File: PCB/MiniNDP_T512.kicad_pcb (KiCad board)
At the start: 2 copper layers, 60 x 34 mm, 25 parts, among them J1 Conn_02x20_Odd_Even, U1 HC238, U2 HC4040, U3 HC573, U4 AS6C4008, U5 1G79, U6 2G00

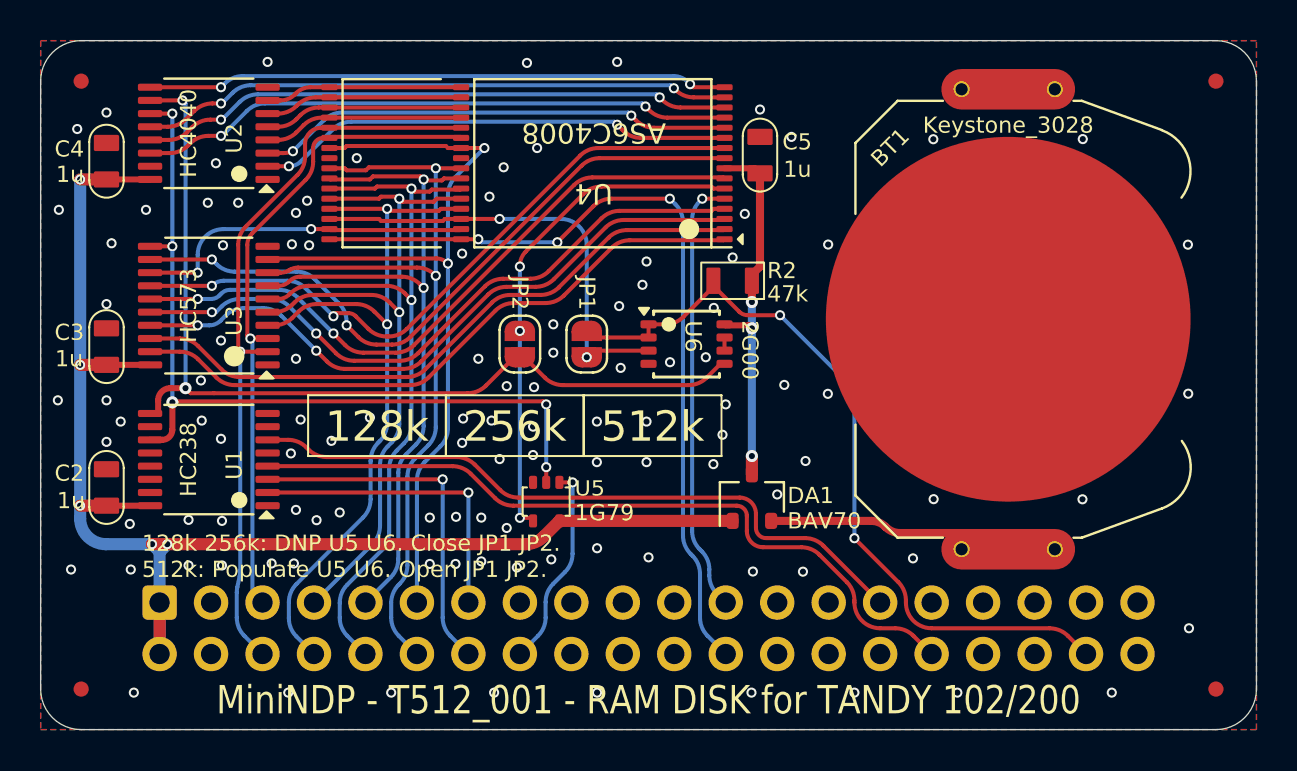
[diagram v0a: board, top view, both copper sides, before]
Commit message: T512 connect all gnd islands
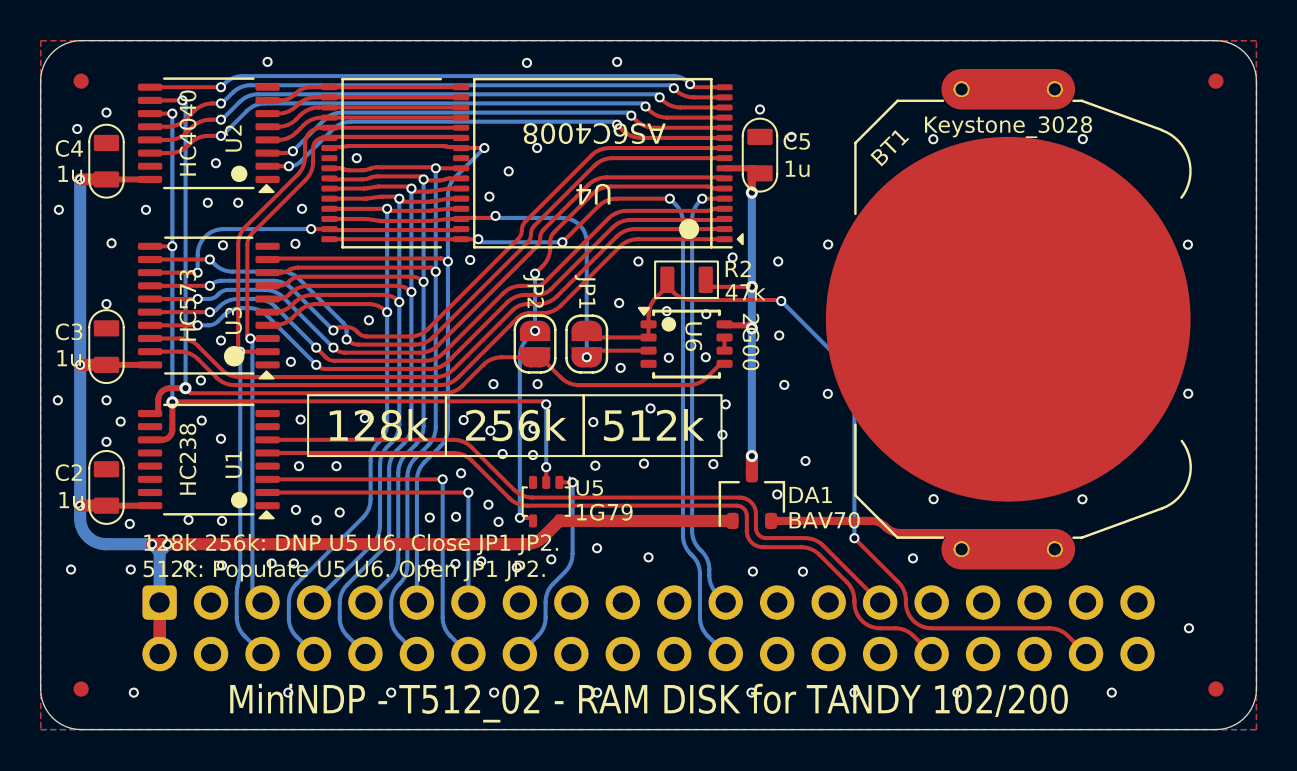
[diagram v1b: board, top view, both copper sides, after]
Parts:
- moved R2 2.28 mm to (153.8, 97.8)
- moved JP2 0.75 mm to (146.3, 101.0)
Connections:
- U1 pad 4: /(A) -> GND
- U1 pad 5: GND -> /(A)
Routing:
- net VMEM: track 18.3 -> 21.0 mm, vias 3 -> 4
- net /RAMRST: track 38.8 -> 39.9 mm
- net GND: vias 111 -> 108

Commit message: T512 power traces
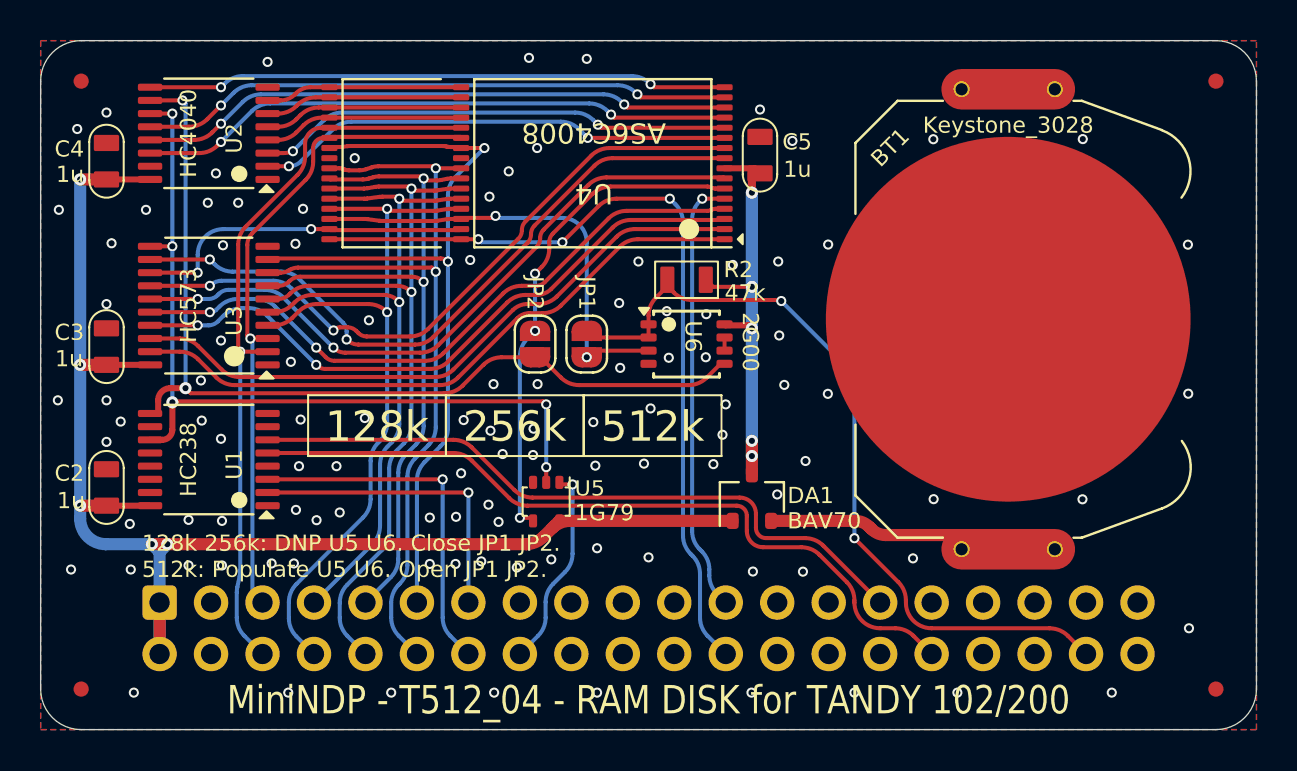
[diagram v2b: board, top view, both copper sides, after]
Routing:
- net +BATT: track 14.5 -> 12.2 mm
- net VMEM: track 21.0 -> 21.7 mm, vias 4 -> 5

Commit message: T512 traces
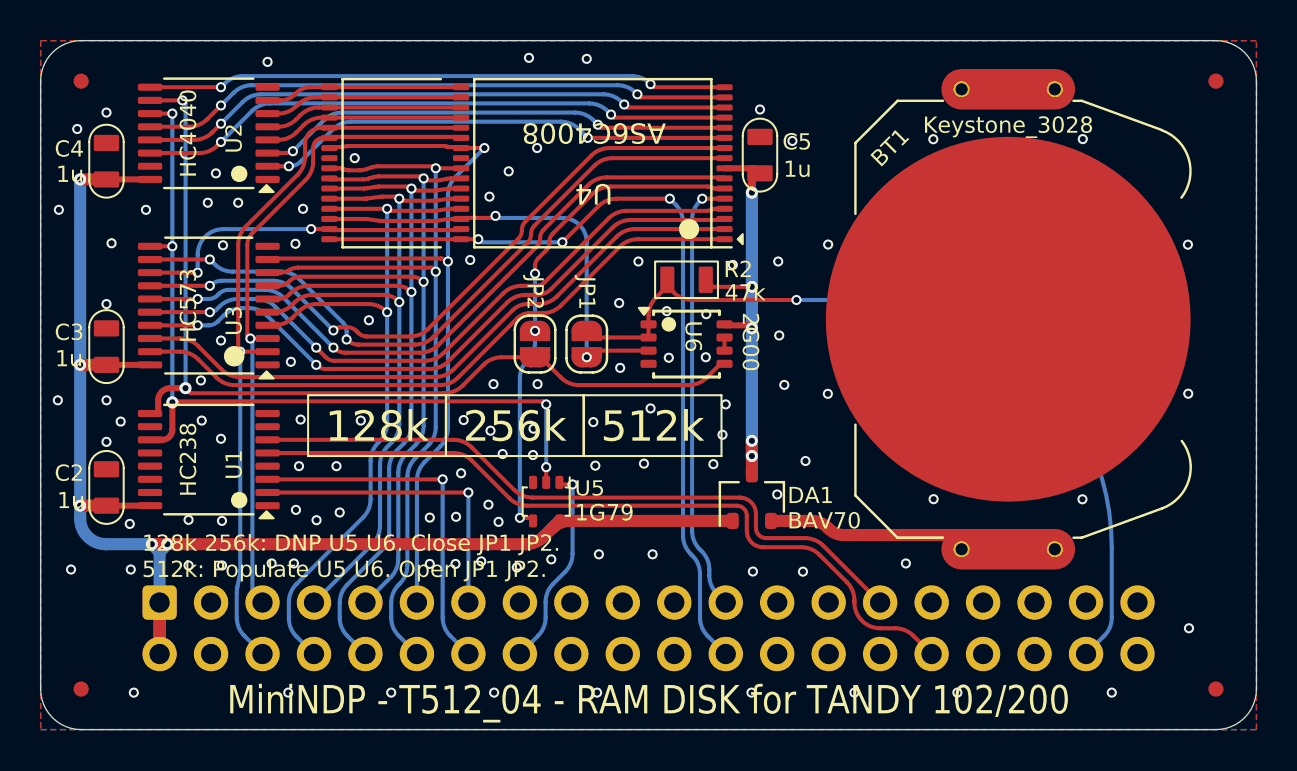
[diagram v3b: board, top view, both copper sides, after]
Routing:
- net /RAMRST: track 39.9 -> 41.0 mm, vias 2 -> 1

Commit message: simplify covers, strengthen battery holders, silkscreen, readme
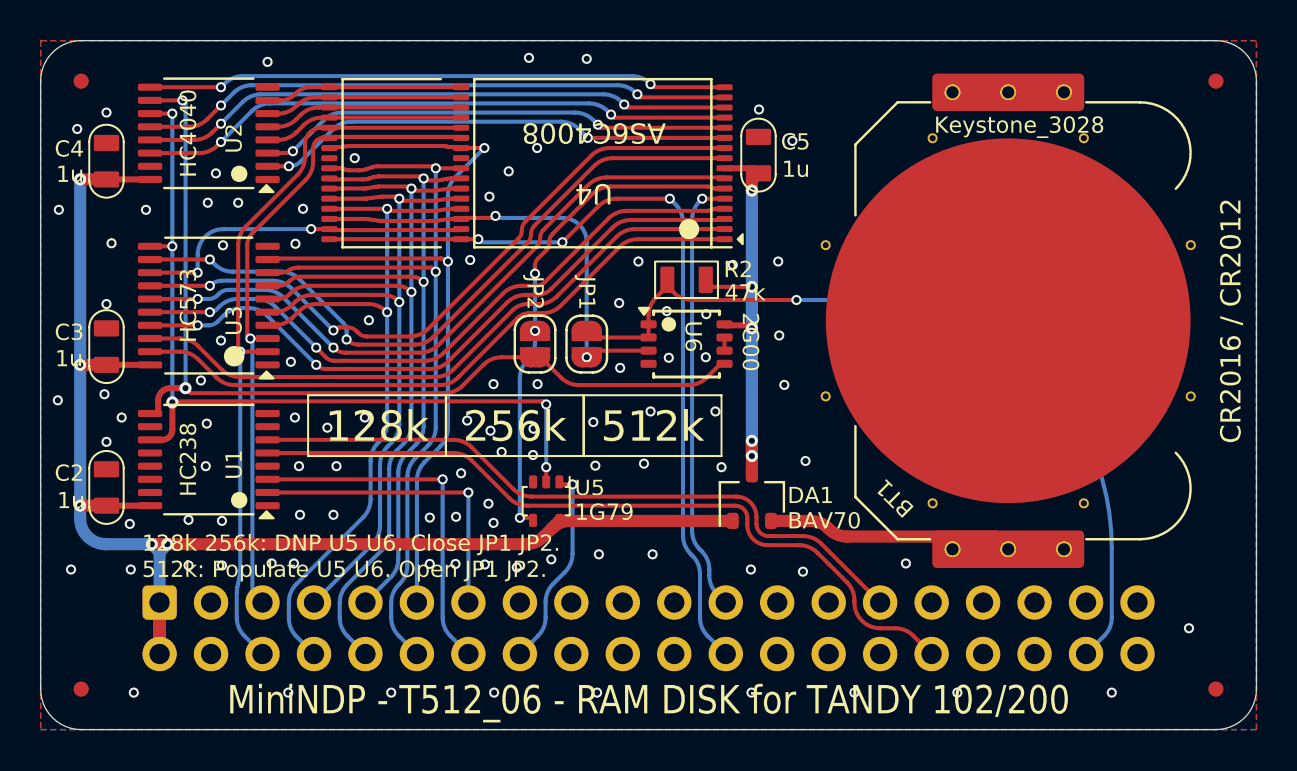
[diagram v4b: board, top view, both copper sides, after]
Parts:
- removed REF** (x4): pth_nail, 000_LOCAL:pth_nail
- BT1: footprint 000_LOCAL:Keystone_3028_3034 -> 000_LOCAL:Keystone_3028_3034_bkw
- moved BT1 0.07 mm to (169.7, 99.8)
- moved C5 0.07 mm to (157.4, 91.7)
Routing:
- net GND: vias 108 -> 98
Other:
- board text added: "BATTERY CR2016 CR2012"
- board text added: "CR2016 / CR2012"
- board text added: "bank 0:P=129 1:P=133 block 0-255: OUT P,N read byte: D=INP(131) write byte: OUT 131,D"
- board text removed: "bank0-3: P=129,133,137,141 block0-255: OUT P,N read byte: N=INP(131) write byte: OUT 131,N"

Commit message: battery holder footprints
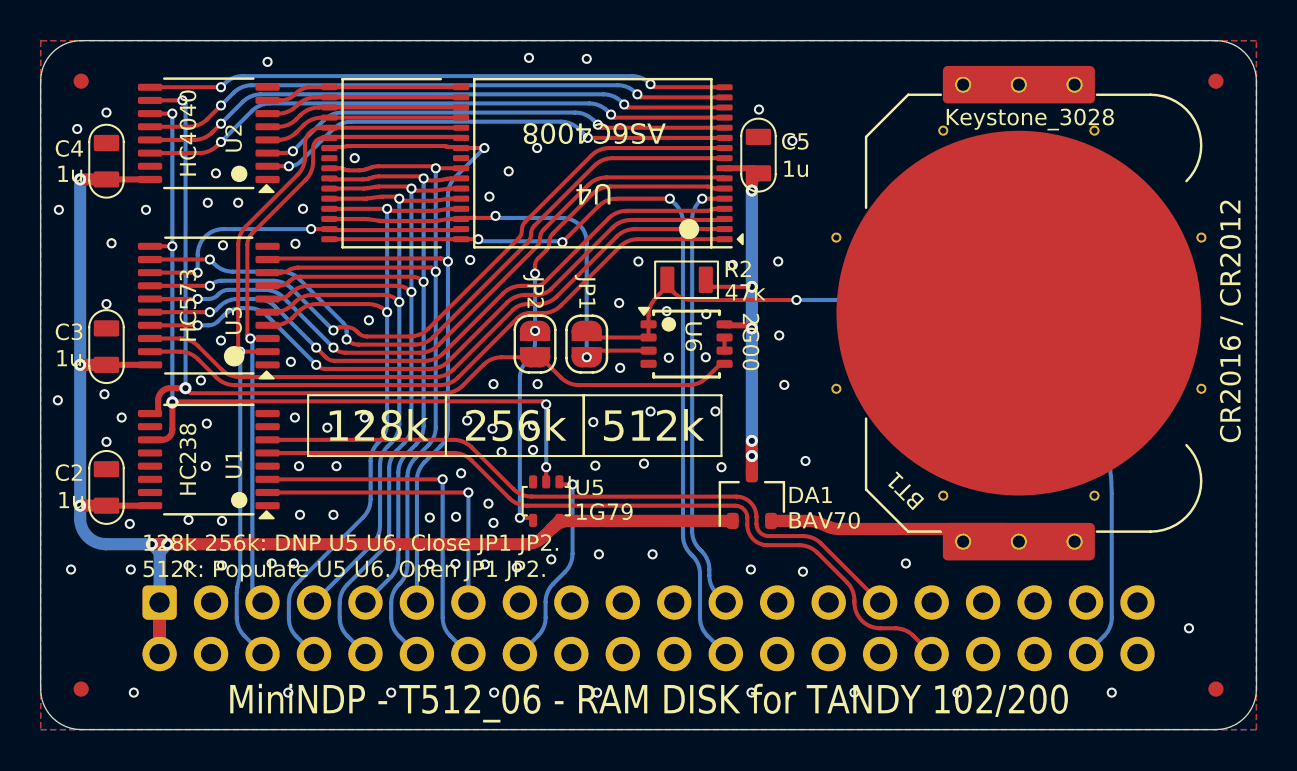
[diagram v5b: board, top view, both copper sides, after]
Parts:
- moved BT1 0.65 mm to (170.2, 99.5)
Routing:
- net /RAMRST: track 41.0 -> 42.3 mm
